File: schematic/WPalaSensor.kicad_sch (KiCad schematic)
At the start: 10 parts, among them J1 WeMos_mini_Hat_Left, J2 WeMos_mini_Hat_Right, J3 Fumis T01, U1 DS18B20, U2 MCP4725

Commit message: Add version to schematic
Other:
- note added: "V3.0"
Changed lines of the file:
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@@
+		)
+	)
+	(text "V3.0"
+		(exclude_from_sim no)
+		(at 30.734 24.13 0)
+		(effects
+			(font
+				(size 2.54 2.54)
+				(thickness 0.508)
+				(bold yes)
+			)
 		)
 	)

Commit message: Add R4
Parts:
- added R4: 2.2K, Resistor_SMD:R_0805_2012Metric_Pad1.20x1.40mm_HandSolder, symbol Device:R
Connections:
- net at J3.2 (Pin_2): now also R4.1; no longer U2.1 (VOUT)
- new net: R4.2, U2.1 (VOUT)
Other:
- moved on the sheet: C1, C2, J1, J2, J3, R1, R2, R3, U1, U2

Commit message: Add C3 capacitor
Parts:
- added C3: 100n, Capacitor_SMD:C_0805_2012Metric_Pad1.18x1.45mm_HandSolder, symbol Device:C
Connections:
- net GND: now also C3.2
- net at R4.2, U2.1 (VOUT): now also C3.1
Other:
- moved on the sheet: C1, C2, J3, R4

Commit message: Update schematic
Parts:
- J3: JlcRotOffset (none) -> 180
- R4: value 2.2K -> 2.2K 1%
- U2: footprint Package_TO_SOT_SMD:SOT-23-6 -> Package_TO_SOT_SMD:SOT-23-6_Handsoldering; JlcRotOffset (none) -> 90
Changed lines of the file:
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@@
+			)
+		)
+		(property "JlcRotOffset" "180"
+			(at 20.32 36.83 0)
+			(effects
+				(font
+					(size 1.27 1.27)
+				)
+				(hide yes)
 			)
 		)
@@
 			)
 		)
-		(property "Footprint" "Package_TO_SOT_SMD:SOT-23-6"
+		(property "Footprint" "Package_TO_SOT_SMD:SOT-23-6_Handsoldering"
 			(at 53.34 40.64 0)
 			(effects
@@
 		)
 		(property "LCSC" "C144198"
+			(at 53.34 34.29 0)
+			(effects
+				(font
+					(size 1.27 1.27)
+				)
+				(hide yes)
+			)
+		)
+		(property "JlcRotOffset" "90"
 			(at 53.34 34.29 0)
 			(effects
@@
 			)
 		)
-		(property "Value" "2.2K"
+		(property "Value" "2.2K 1%"
 			(at 30.48 31.75 90)
 			(effects

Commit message: Copy MCP4725 schematic symbol locally
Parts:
- U2: symbol Analog_DAC:MCP4725xxx-xCH -> MCP4725:MCP4725xxx-xCH
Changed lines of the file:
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@@
 	)
 	(symbol
-		(lib_id "Analog_DAC:MCP4725xxx-xCH")
+		(lib_id "MCP4725:MCP4725xxx-xCH")
 		(at 53.34 34.29 0)
 		(mirror y)

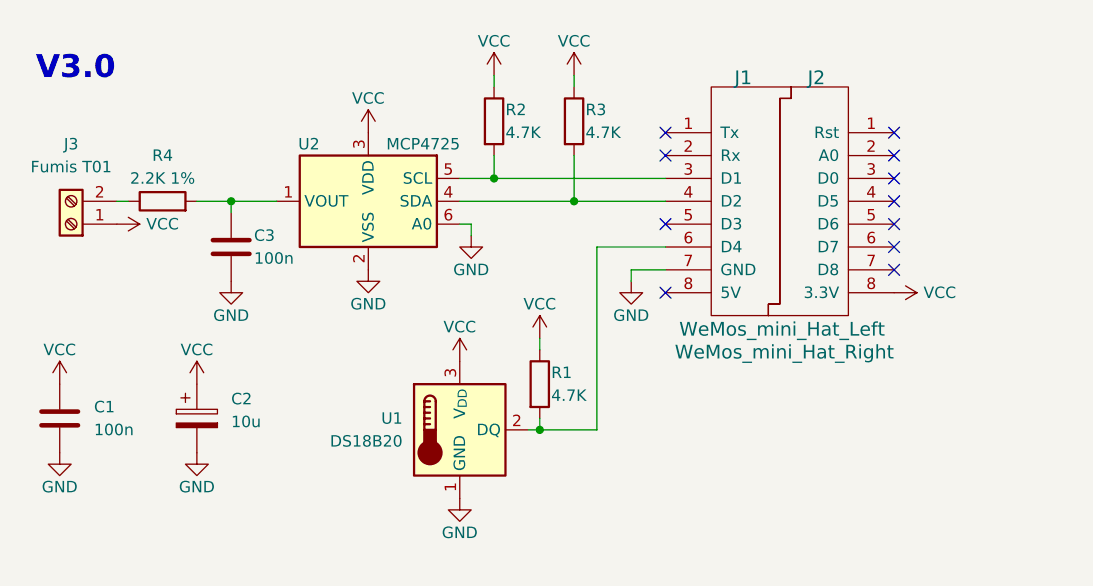
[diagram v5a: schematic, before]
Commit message: Adjust schematic to use MCP4726
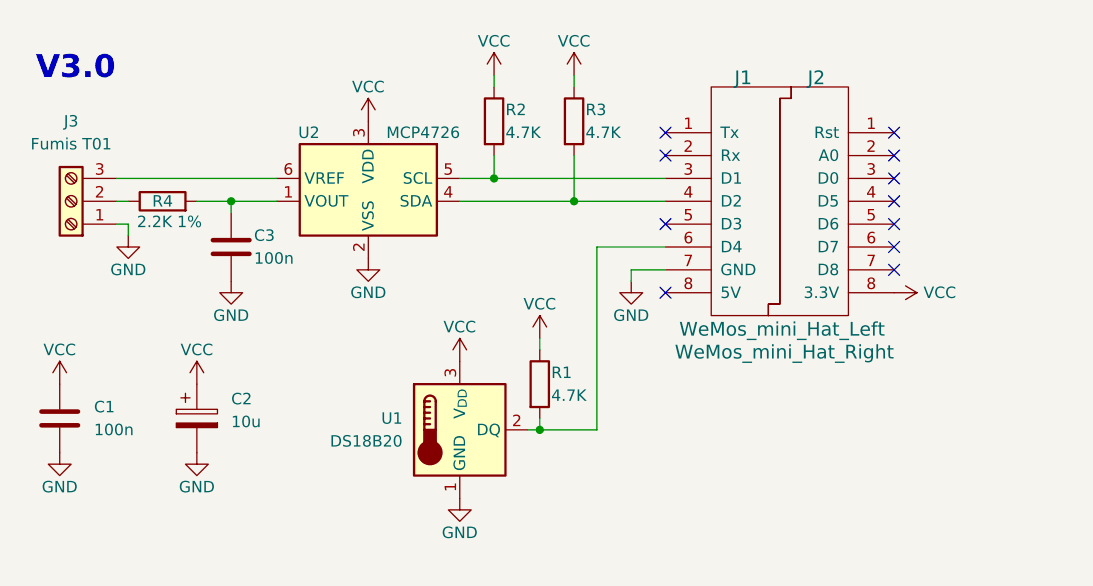
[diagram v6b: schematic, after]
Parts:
- J3: footprint TerminalBlock:TerminalBlock_bornier-2_P5.08mm -> TerminalBlock:TerminalBlock_bornier-3_P5.08mm; symbol Connector:Screw_Terminal_01x02 -> Connector:Screw_Terminal_01x03; LCSC C474881 -> C474882
- U2: value MCP4725 -> MCP4726; symbol MCP4725:MCP4725xxx-xCH -> MCP47X6:MCP47X6xxx-xCH; LCSC C144198 -> C191581
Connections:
- net GND: now also J3.1 (Pin_1); no longer U2.6 (A0)
- net VCC: no longer J3.1 (Pin_1)
- new net: J3.3 (Pin_3), U2.6 (VREF)
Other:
- moved on the sheet: U2
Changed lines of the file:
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@@
 	(wire
 		(pts
-			(xy 63.5 36.83) (xy 64.77 36.83)
+			(xy 25.4 36.83) (xy 26.67 36.83)
 		)
 		(stroke
@@
 	(wire
 		(pts
-			(xy 64.77 36.83) (xy 64.77 38.1)
+			(xy 26.67 36.83) (xy 26.67 38.1)
 		)
 		(stroke
@@
 		(pts
 			(xy 86.36 39.37) (xy 78.74 39.37)
+		)
+		(stroke
+			(width 0)
+			(type default)
+		)
+	)
+	(wire
+		(pts
+			(xy 25.4 31.75) (xy 43.18 31.75)
 		)
 		(stroke
@@
 	(symbol
 		(lib_id "power:VCC")
-		(at 53.34 26.67 0)
+		(at 53.34 25.4 0)
 		(unit 1)
 		(exclude_from_sim no)
@@
 		(dnp no)
 		(property "Reference" "#PWR09"
-			(at 53.34 30.48 0)
+			(at 53.34 29.21 0)
 			(effects
 				(font
@@
 		)
 		(property "Value" "VCC"
-			(at 53.34 22.86 0)
+			(at 53.34 21.59 0)
 			(effects
 				(font
@@
 		)
 		(property "Footprint" ""
-			(at 53.34 26.67 0)
+			(at 53.34 25.4 0)
 			(effects
 				(font
@@
 		)
 		(property "Datasheet" ""
-			(at 53.34 26.67 0)
+			(at 53.34 25.4 0)
 			(effects
 				(font
@@
 		)
 		(property "Description" ""
-			(at 53.34 26.67 0)
+			(at 53.34 25.4 0)
 			(effects
 				(font
@@
 	(symbol
 		(lib_id "power:GND")
-		(at 53.34 41.91 0)
+		(at 53.34 40.64 0)
 		(unit 1)
 		(exclude_from_sim no)
@@
 		(dnp no)
 		(property "Reference" "#PWR08"
-			(at 53.34 48.26 0)
+			(at 53.34 46.99 0)
 			(effects
 				(font
@@
 		)
 		(property "Value" "GND"
-			(at 53.34 45.72 0)
+			(at 53.34 44.45 0)
 			(effects
 				(font
@@
 		)
 		(property "Footprint" ""
-			(at 53.34 41.91 0)
+			(at 53.34 40.64 0)
 			(effects
 				(font
@@
 		)
 		(property "Datasheet" ""
-			(at 53.34 41.91 0)
+			(at 53.34 40.64 0)
 			(effects
 				(font
@@
 		)
 		(property "Description" ""
-			(at 53.34 41.91 0)
+			(at 53.34 40.64 0)
 			(effects
 				(font
@@
 				(path "/33440f6f-72cd-41c2-99cf-599b7ace8c73"
 					(reference "#PWR08")
-					(unit 1)
-				)
-			)
-		)
-	)
-	(symbol
-		(lib_id "power:VCC")
-		(at 25.4 36.83 270)
-		(unit 1)
-		(exclude_from_sim no)
-		(in_bom yes)
-		(on_board yes)
-		(dnp no)
-		(property "Reference" "#PWR011"
-			(at 21.59 36.83 0)
-			(effects
-				(font
-					(size 1.27 1.27)
-				)
-				(hide yes)
-			)
-		)
-		(property "Value" "VCC"
-			(at 30.48 36.83 90)
-			(effects
-				(font
-					(size 1.27 1.27)
-				)
-			)
-		)
-		(property "Footprint" ""
-			(at 25.4 36.83 0)
-			(effects
-				(font
-					(size 1.27 1.27)
-				)
-			)
-		)
-		(property "Datasheet" ""
-			(at 25.4 36.83 0)
-			(effects
-				(font
-					(size 1.27 1.27)
-				)
-			)
-		)
-		(property "Description" ""
-			(at 25.4 36.83 0)
-			(effects
-				(font
-					(size 1.27 1.27)
-				)
-				(hide yes)
-			)
-		)
-		(pin "1"
-		)
-		(instances
-			(project "WPalaSensor"
-				(path "/33440f6f-72cd-41c2-99cf-599b7ace8c73"
-					(reference "#PWR011")
 					(unit 1)
 				)
@@
 	)
 	(symbol
-		(lib_id "Connector:Screw_Terminal_01x02")
-		(at 20.32 36.83 180)
+		(lib_id "Connector:Screw_Terminal_01x03")
+		(at 20.32 34.29 180)
 		(unit 1)
 		(exclude_from_sim no)
@@
 		(fields_autoplaced yes)
 		(property "Reference" "J3"
+			(at 20.32 25.4 0)
+			(effects
+				(font
+					(size 1.27 1.27)
+				)
+			)
+		)
+		(property "Value" "Fumis T01"
 			(at 20.32 27.94 0)
 			(effects
@@
 			)
 		)
-		(property "Value" "Fumis T01"
-			(at 20.32 30.48 0)
-			(effects
-				(font
-					(size 1.27 1.27)
-				)
-			)
-		)
-		(property "Footprint" "TerminalBlock:TerminalBlock_bornier-2_P5.08mm"
-			(at 20.32 36.83 0)
+		(property "Footprint" "TerminalBlock:TerminalBlock_bornier-3_P5.08mm"
+			(at 20.32 34.29 0)
 			(effects
 				(font
@@
 		)
 		(property "Datasheet" "~"
-			(at 20.32 36.83 0)
-			(effects
-				(font
-					(size 1.27 1.27)
-				)
-				(hide yes)
-			)
-		)
-		(property "Description" "Generic screw terminal, single row, 01x02, script generated (kicad-library-utils/schlib/autogen/connector/)"
-			(at 20.32 36.83 0)
-			(effects
-				(font
-					(size 1.27 1.27)
-				)
-				(hide yes)
-			)
-		)
-		(property "LCSC" "C474881"
-			(at 20.32 36.83 0)
+			(at 20.32 34.29 0)
+			(effects
+				(font
+					(size 1.27 1.27)
+				)
+				(hide yes)
+			)
+		)
+		(property "Description" "Generic screw terminal, single row, 01x03, script generated (kicad-library-utils/schlib/autogen/connector/)"
+			(at 20.32 34.29 0)
+			(effects
+				(font
+					(size 1.27 1.27)
+				)
+				(hide yes)
+			)
+		)
+		(property "LCSC" "C474882"
+			(at 20.32 34.29 0)
 			(effects
 				(font
@@
 		)
 		(property "JlcRotOffset" "180"
-			(at 20.32 36.83 0)
+			(at 20.32 34.29 0)
 			(effects
 				(font
@@
 		(pin "1"
 		)
+		(pin "3"
+		)
 		(instances
 			(project ""
@@
 	(symbol
 		(lib_id "power:GND")
-		(at 64.77 38.1 0)
+		(at 26.67 38.1 0)
 		(unit 1)
 		(exclude_from_sim no)
@@
 		(dnp no)
 		(property "Reference" "#PWR06"
-			(at 64.77 44.45 0)
+			(at 26.67 44.45 0)
 			(effects
 				(font
@@
 		)
 		(property "Value" "GND"
-			(at 64.77 41.91 0)
+			(at 26.67 41.91 0)
 			(effects
 				(font
@@
 		)
 		(property "Footprint" ""
-			(at 64.77 38.1 0)
+			(at 26.67 38.1 0)
 			(effects
 				(font
@@
 		)
 		(property "Datasheet" ""
-			(at 64.77 38.1 0)
+			(at 26.67 38.1 0)
 			(effects
 				(font
@@
 		)
 		(property "Description" ""
-			(at 64.77 38.1 0)
+			(at 26.67 38.1 0)
 			(effects
 				(font
@@
 	)
 	(symbol
-		(lib_id "MCP4725:MCP4725xxx-xCH")
-		(at 53.34 34.29 0)
+		(lib_id "MCP47X6:MCP47X6xxx-xCH")
+		(at 53.34 33.02 0)
 		(mirror y)
 		(unit 1)
@@
 		(dnp no)
 		(property "Reference" "U2"
-			(at 46.736 27.94 0)
-			(effects
-				(font
-					(size 1.27 1.27)
-				)
-			)
-		)
-		(property "Value" "MCP4725"
-			(at 59.436 27.94 0)
+			(at 46.736 26.67 0)
+			(effects
+				(font
+					(size 1.27 1.27)
+				)
+			)
+		)
+		(property "Value" "MCP4726"
+			(at 59.436 26.67 0)
 			(effects
 				(font
@@
 		)
 		(property "Footprint" "Package_TO_SOT_SMD:SOT-23-6_Handsoldering"
-			(at 53.34 40.64 0)
-			(effects
-				(font
-					(size 1.27 1.27)
-				)
-				(hide yes)
-			)
-		)
-		(property "Datasheet" "http://ww1.microchip.com/downloads/en/DeviceDoc/22039d.pdf"
-			(at 53.34 34.29 0)
+			(at 53.34 39.37 0)
+			(effects
+				(font
+					(size 1.27 1.27)
+				)
+				(hide yes)
+			)
+		)
+		(property "Datasheet" "https://ww1.microchip.com/downloads/aemDocuments/documents/OTH/ProductDocuments/DataSheets/22272C.pdf"
+			(at 53.34 33.02 0)
 			(effects
 				(font
@@
 		)
 		(property "Description" "12-bit Digital-to-Analog Converter, integrated EEPROM, I2C interface, SOT-23-6"
-			(at 53.34 34.29 0)
-			(effects
-				(font
-					(size 1.27 1.27)
-				)
-				(hide yes)
-			)
-		)
-		(property "LCSC" "C144198"
-			(at 53.34 34.29 0)
+			(at 53.34 33.02 0)
+			(effects
+				(font
+					(size 1.27 1.27)
+				)
+				(hide yes)
+			)
+		)
+		(property "LCSC" "C191581"
+			(at 53.34 33.02 0)
 			(effects
 				(font
@@
 		)
 		(property "JlcRotOffset" "90"
-			(at 53.34 34.29 0)
+			(at 53.34 33.02 0)
 			(effects
 				(font
@@
 		(dnp no)
 		(property "Reference" "R4"
-			(at 30.48 29.21 90)
+			(at 30.48 34.29 90)
 			(effects
 				(font
@@
 		)
 		(property "Value" "2.2K 1%"
-			(at 30.48 31.75 90)
-			(effects
-				(font
+			(at 31.242 36.576 90)
+			(effects
+				(font

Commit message: Remove C3
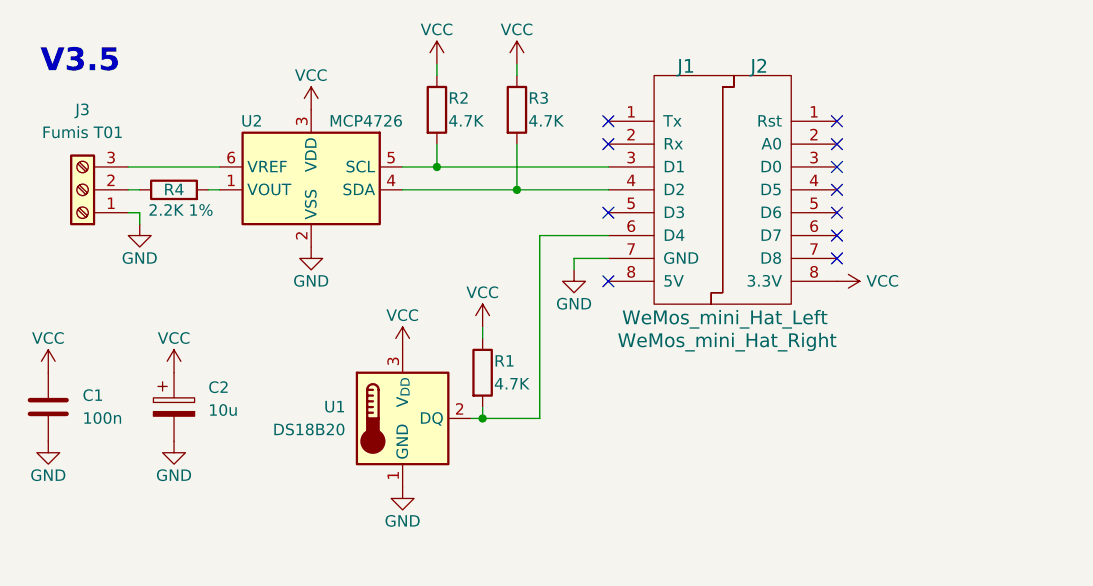
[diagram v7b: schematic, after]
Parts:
- removed C3: 100n, Capacitor_SMD:C_0805_2012Metric_Pad1.18x1.45mm_HandSolder, symbol Device:C
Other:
- note added: "V3.5"
- note removed: "V3.0"
- moved on the sheet: C1, C2, J1, J2, J3, R1, R2, R3, R4, U1, U2
